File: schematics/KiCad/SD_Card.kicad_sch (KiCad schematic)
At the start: 13 parts, among them J6 Micro_SD_Card_Det_Hirose_DM3AT, U14 LP2950-3.3, U16 74HC4050

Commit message: Update schematics.
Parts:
- renumbered R19 to R20, R20 to R21, R21 to R22, R22 to R23, R23 to R24
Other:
- company: (none) -> By 46nori
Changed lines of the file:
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@@
   (title_block
     (title "Micro SD Card interface")
+    (date "2023-05-03")
+    (company "By 46nori")
   )
   (junction (at 43.18 143.51) (diameter 0) (color 0 0 0 0)
@@
   (symbol (lib_id "power:GND") (at 125.73 71.12 0) (unit 1)
     (in_bom yes) (on_board yes) (dnp no)
-    (property "Reference" "#PWR074" (at 125.73 77.47 0)
+    (property "Reference" "#PWR076" (at 125.73 77.47 0)
       (effects (font (size 1.27 1.27)) hide)
     )
@@
       (project "Z80ATmega128"
         (path "/8c0ff608-9e5b-458c-8fa7-b9973ff97e88/07de70fd-23a2-48ea-a888-9c9311d1e8a8"
-          (reference "#PWR074") (unit 1)
+          (reference "#PWR076") (unit 1)
         )
       )
@@
   (symbol (lib_id "power:GND") (at 73.66 96.52 0) (unit 1)
     (in_bom yes) (on_board yes) (dnp no) (fields_autoplaced)
-    (property "Reference" "#PWR075" (at 73.66 102.87 0)
+    (property "Reference" "#PWR077" (at 73.66 102.87 0)
       (effects (font (size 1.27 1.27)) hide)
     )
@@
       (project "Z80ATmega128"
         (path "/8c0ff608-9e5b-458c-8fa7-b9973ff97e88/07de70fd-23a2-48ea-a888-9c9311d1e8a8"
-          (reference "#PWR075") (unit 1)
+          (reference "#PWR077") (unit 1)
         )
       )
@@
   (symbol (lib_id "power:GND") (at 148.59 168.91 0) (unit 1)
     (in_bom yes) (on_board yes) (dnp no) (fields_autoplaced)
-    (property "Reference" "#PWR081" (at 148.59 175.26 0)
+    (property "Reference" "#PWR083" (at 148.59 175.26 0)
       (effects (font (size 1.27 1.27)) hide)
     )
@@
       (project "Z80ATmega128"
         (path "/8c0ff608-9e5b-458c-8fa7-b9973ff97e88/07de70fd-23a2-48ea-a888-9c9311d1e8a8"
-          (reference "#PWR081") (unit 1)
+          (reference "#PWR083") (unit 1)
         )
       )
@@
   (symbol (lib_id "Device:R") (at 90.17 44.45 0) (unit 1)
     (in_bom yes) (on_board yes) (dnp no) (fields_autoplaced)
-    (property "Reference" "R19" (at 92.71 43.1799 0)
+    (property "Reference" "R20" (at 92.71 43.1799 0)
       (effects (font (size 1.27 1.27)) (justify left))
     )
@@
       (project "Z80ATmega128"
         (path "/8c0ff608-9e5b-458c-8fa7-b9973ff97e88/07de70fd-23a2-48ea-a888-9c9311d1e8a8"
-          (reference "R19") (unit 1)
+          (reference "R20") (unit 1)
         )
       )
@@
   (symbol (lib_id "power:+3.3V") (at 123.19 146.05 0) (unit 1)
     (in_bom yes) (on_board yes) (dnp no) (fields_autoplaced)
-    (property "Reference" "#PWR080" (at 123.19 149.86 0)
+    (property "Reference" "#PWR082" (at 123.19 149.86 0)
       (effects (font (size 1.27 1.27)) hide)
     )
@@
       (project "Z80ATmega128"
         (path "/8c0ff608-9e5b-458c-8fa7-b9973ff97e88/07de70fd-23a2-48ea-a888-9c9311d1e8a8"
-          (reference "#PWR080") (unit 1)
+          (reference "#PWR082") (unit 1)
         )
       )
@@
   (symbol (lib_id "Device:R") (at 148.59 95.25 0) (unit 1)
     (in_bom yes) (on_board yes) (dnp no) (fields_autoplaced)
-    (property "Reference" "R22" (at 151.13 93.9799 0)
+    (property "Reference" "R23" (at 151.13 93.9799 0)
       (effects (font (size 1.27 1.27)) (justify left))
     )
@@
       (project "Z80ATmega128"
         (path "/8c0ff608-9e5b-458c-8fa7-b9973ff97e88/07de70fd-23a2-48ea-a888-9c9311d1e8a8"
-          (reference "R22") (unit 1)
+          (reference "R23") (unit 1)
         )
       )
@@
         )
         (path "/8c0ff608-9e5b-458c-8fa7-b9973ff97e88/07de70fd-23a2-48ea-a888-9c9311d1e8a8"
-          (reference "#PWR079") (unit 1)
+          (reference "#PWR081") (unit 1)
         )
       )
@@
   (symbol (lib_id "power:+3.3V") (at 73.66 40.64 0) (unit 1)
     (in_bom yes) (on_board yes) (dnp no)
-    (property "Reference" "#PWR071" (at 73.66 44.45 0)
+    (property "Reference" "#PWR073" (at 73.66 44.45 0)
       (effects (font (size 1.27 1.27)) hide)
     )
@@
       (project "Z80ATmega128"
         (path "/8c0ff608-9e5b-458c-8fa7-b9973ff97e88/07de70fd-23a2-48ea-a888-9c9311d1e8a8"
-          (reference "#PWR071") (unit 1)
+          (reference "#PWR073") (unit 1)
         )
       )
@@
   (symbol (lib_id "Device:R") (at 125.73 44.45 0) (unit 1)
     (in_bom yes) (on_board yes) (dnp no) (fields_autoplaced)
-    (property "Reference" "R20" (at 128.27 43.1799 0)
+    (property "Reference" "R21" (at 128.27 43.1799 0)
       (effects (font (size 1.27 1.27)) (justify left))
     )
@@
       (project "Z80ATmega128"
         (path "/8c0ff608-9e5b-458c-8fa7-b9973ff97e88/07de70fd-23a2-48ea-a888-9c9311d1e8a8"
-          (reference "R20") (unit 1)
+          (reference "R21") (unit 1)
         )
       )
@@
   (symbol (lib_id "Device:R") (at 116.84 100.33 270) (unit 1)
     (in_bom yes) (on_board yes) (dnp no) (fields_autoplaced)
-    (property "Reference" "R23" (at 116.84 93.98 90)
+    (property "Reference" "R24" (at 116.84 93.98 90)
       (effects (font (size 1.27 1.27)))
     )
@@
       (project "Z80ATmega128"
         (path "/8c0ff608-9e5b-458c-8fa7-b9973ff97e88/07de70fd-23a2-48ea-a888-9c9311d1e8a8"
-          (reference "R23") (unit 1)
+          (reference "R24") (unit 1)
         )
       )
@@
   (symbol (lib_id "power:VCC") (at 125.73 40.64 0) (unit 1)
     (in_bom yes) (on_board yes) (dnp no) (fields_autoplaced)
-    (property "Reference" "#PWR073" (at 125.73 44.45 0)
+    (property "Reference" "#PWR075" (at 125.73 44.45 0)
       (effects (font (size 1.27 1.27)) hide)
     )
@@
       (project "Z80ATmega128"
         (path "/8c0ff608-9e5b-458c-8fa7-b9973ff97e88/07de70fd-23a2-48ea-a888-9c9311d1e8a8"
-          (reference "#PWR073") (unit 1)
+          (reference "#PWR075") (unit 1)
         )
       )
@@
         )
         (path "/8c0ff608-9e5b-458c-8fa7-b9973ff97e88/07de70fd-23a2-48ea-a888-9c9311d1e8a8"
-          (reference "#PWR077") (unit 1)
+          (reference "#PWR079") (unit 1)
         )
       )
@@
   (symbol (lib_id "Device:R") (at 125.73 67.31 0) (unit 1)
     (in_bom yes) (on_board yes) (dnp no) (fields_autoplaced)
-    (property "Reference" "R21" (at 128.27 66.0399 0)
+    (property "Reference" "R22" (at 128.27 66.0399 0)
       (effects (font (size 1.27 1.27)) (justify left))
     )
@@
       (project "Z80ATmega128"
         (path "/8c0ff608-9e5b-458c-8fa7-b9973ff97e88/07de70fd-23a2-48ea-a888-9c9311d1e8a8"
-          (reference "R21") (unit 1)
+          (reference "R22") (unit 1)
         )
       )
@@
   (symbol (lib_id "power:GND") (at 123.19 171.45 0) (unit 1)
     (in_bom yes) (on_board yes) (dnp no) (fields_autoplaced)
-    (property "Reference" "#PWR082" (at 123.19 177.8 0)
+    (property "Reference" "#PWR084" (at 123.19 177.8 0)
       (effects (font (size 1.27 1.27)) hide)
     )
@@
       (project "Z80ATmega128"
         (path "/8c0ff608-9e5b-458c-8fa7-b9973ff97e88/07de70fd-23a2-48ea-a888-9c9311d1e8a8"
-          (reference "#PWR082") (unit 1)
+          (reference "#PWR084") (unit 1)
         )
       )
@@
   (symbol (lib_id "power:GND") (at 148.59 100.33 0) (unit 1)
     (in_bom yes) (on_board yes) (dnp no) (fields_autoplaced)
-    (property "Reference" "#PWR076" (at 148.59 106.68 0)
+    (property "Reference" "#PWR078" (at 148.59 106.68 0)
       (effects (font (size 1.27 1.27)) hide)
     )
@@
       (project "Z80ATmega128"
         (path "/8c0ff608-9e5b-458c-8fa7-b9973ff97e88/07de70fd-23a2-48ea-a888-9c9311d1e8a8"
-          (reference "#PWR076") (unit 1)
+          (reference "#PWR078") (unit 1)
         )
       )
@@
   (symbol (lib_id "power:VCC") (at 90.17 40.64 0) (unit 1)
     (in_bom yes) (on_board yes) (dnp no)
-    (property "Reference" "#PWR072" (at 90.17 44.45 0)
+    (property "Reference" "#PWR074" (at 90.17 44.45 0)
       (effects (font (size 1.27 1.27)) hide)
     )
@@
       (project "Z80ATmega128"
         (path "/8c0ff608-9e5b-458c-8fa7-b9973ff97e88/07de70fd-23a2-48ea-a888-9c9311d1e8a8"
-          (reference "#PWR072") (unit 1)
+          (reference "#PWR074") (unit 1)
         )
       )
@@
         )
         (path "/8c0ff608-9e5b-458c-8fa7-b9973ff97e88/07de70fd-23a2-48ea-a888-9c9311d1e8a8"
-          (reference "#PWR078") (unit 1)
-        )
-      )
+          (reference "#PWR080") (unit 1)
+        )
+      )

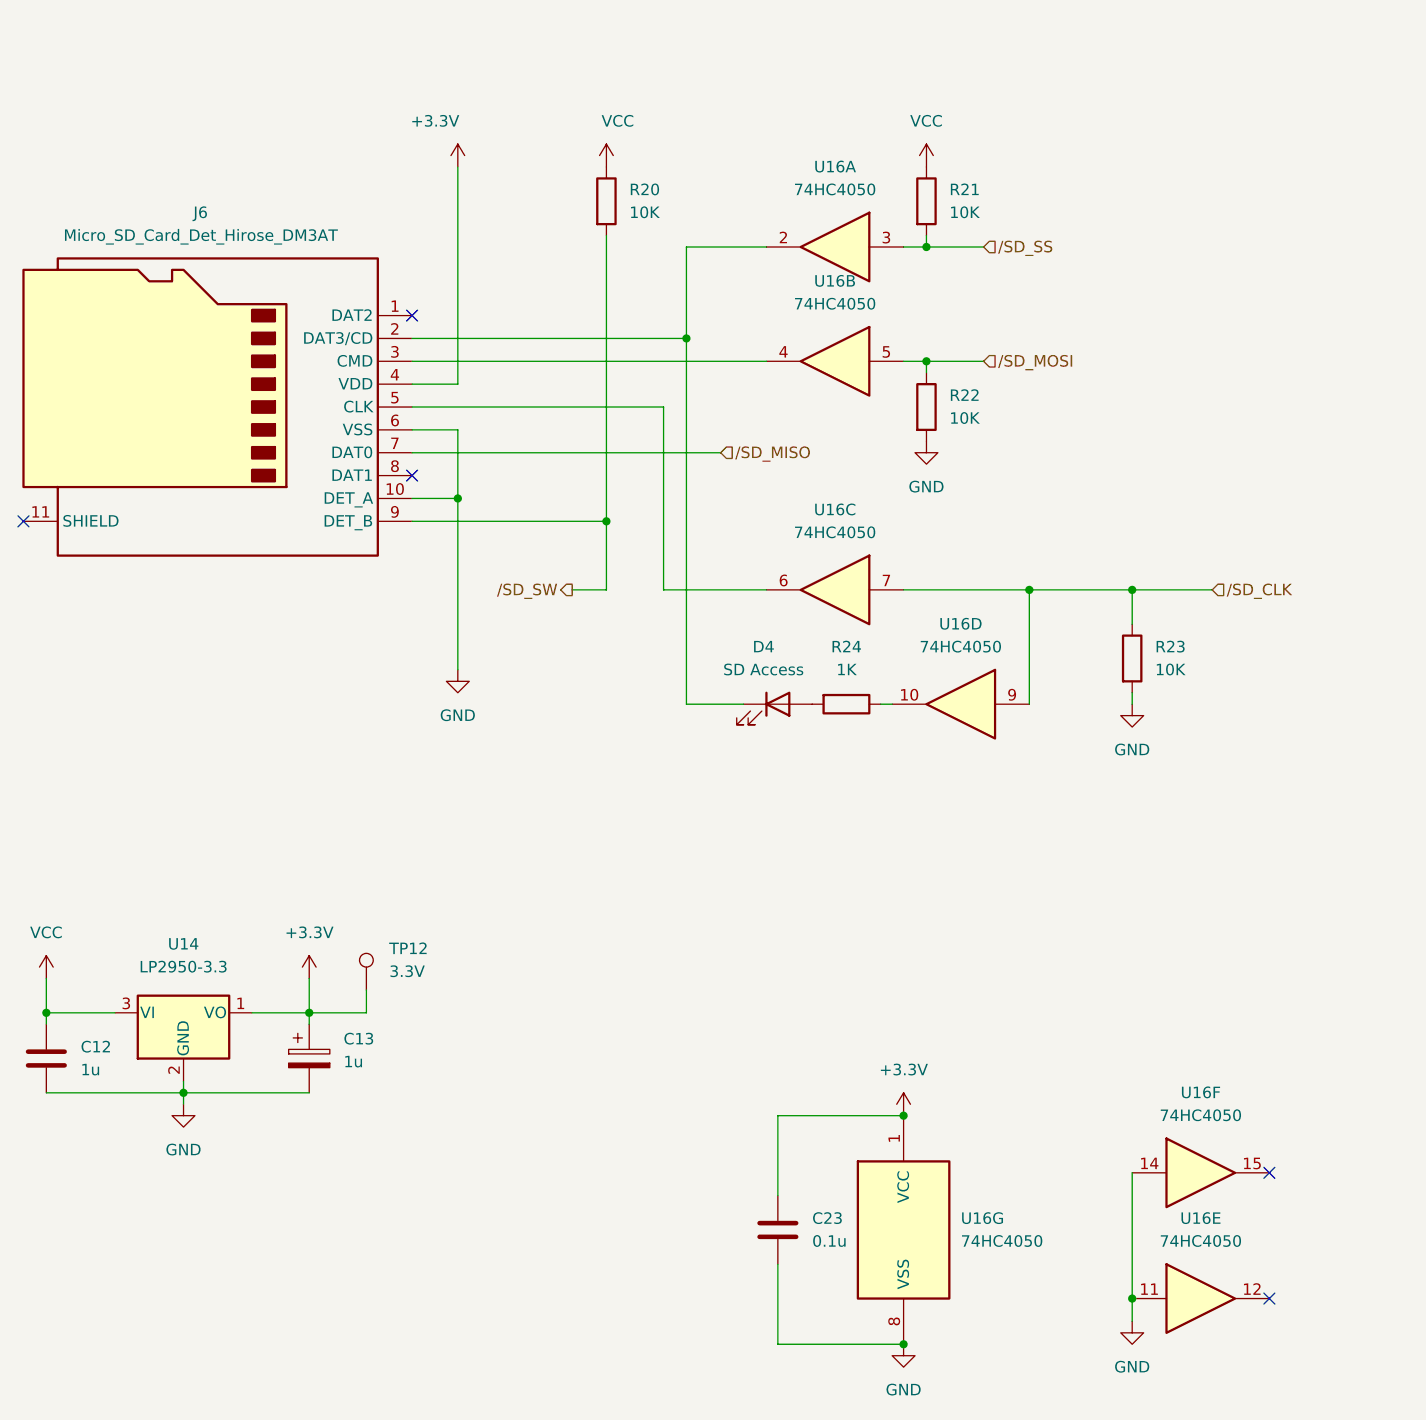
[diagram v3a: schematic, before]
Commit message: Update RESET circuit using DS1232N.
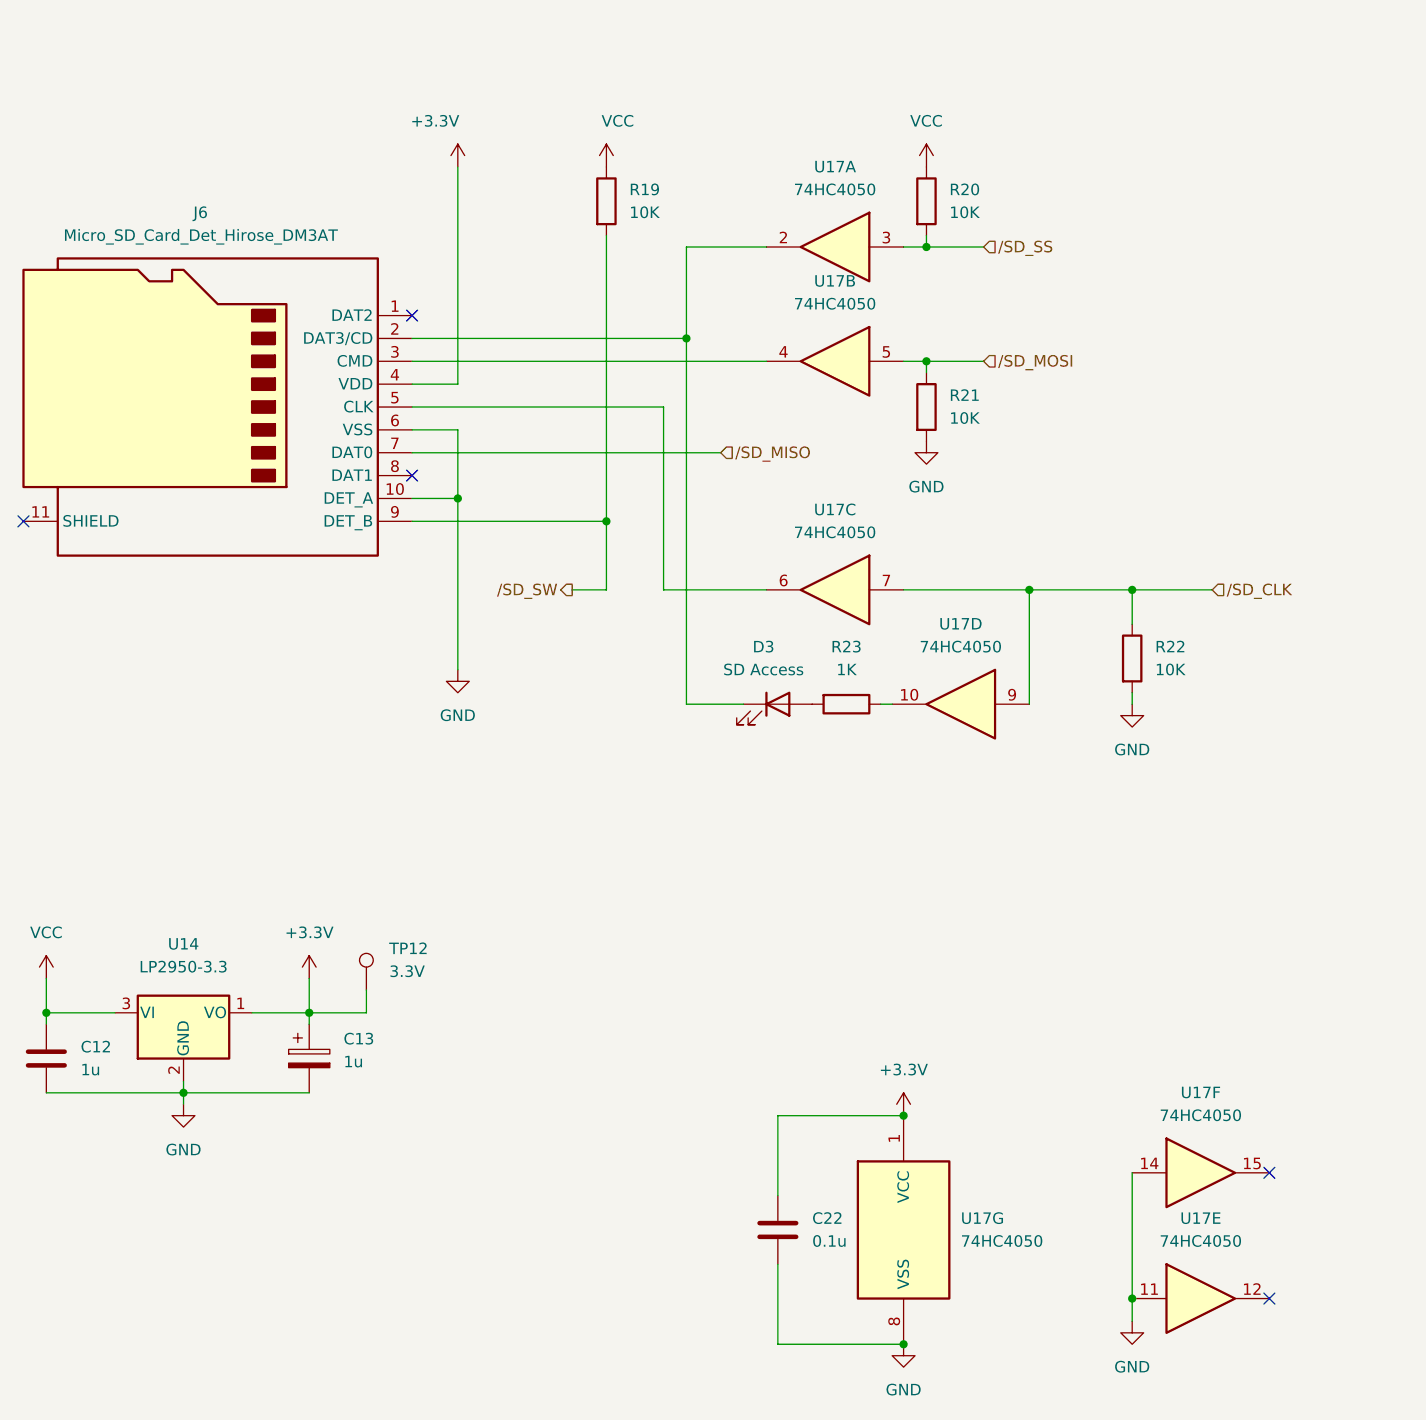
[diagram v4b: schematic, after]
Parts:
- renumbered C23 to C22, D4 to D3, R20 to R19, R21 to R20, R22 to R21, R23 to R22, R24 to R23, U16 to U17

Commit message: Fixed bug of WAIT generator circuit
Clock circuit is moved to 2nd layer.
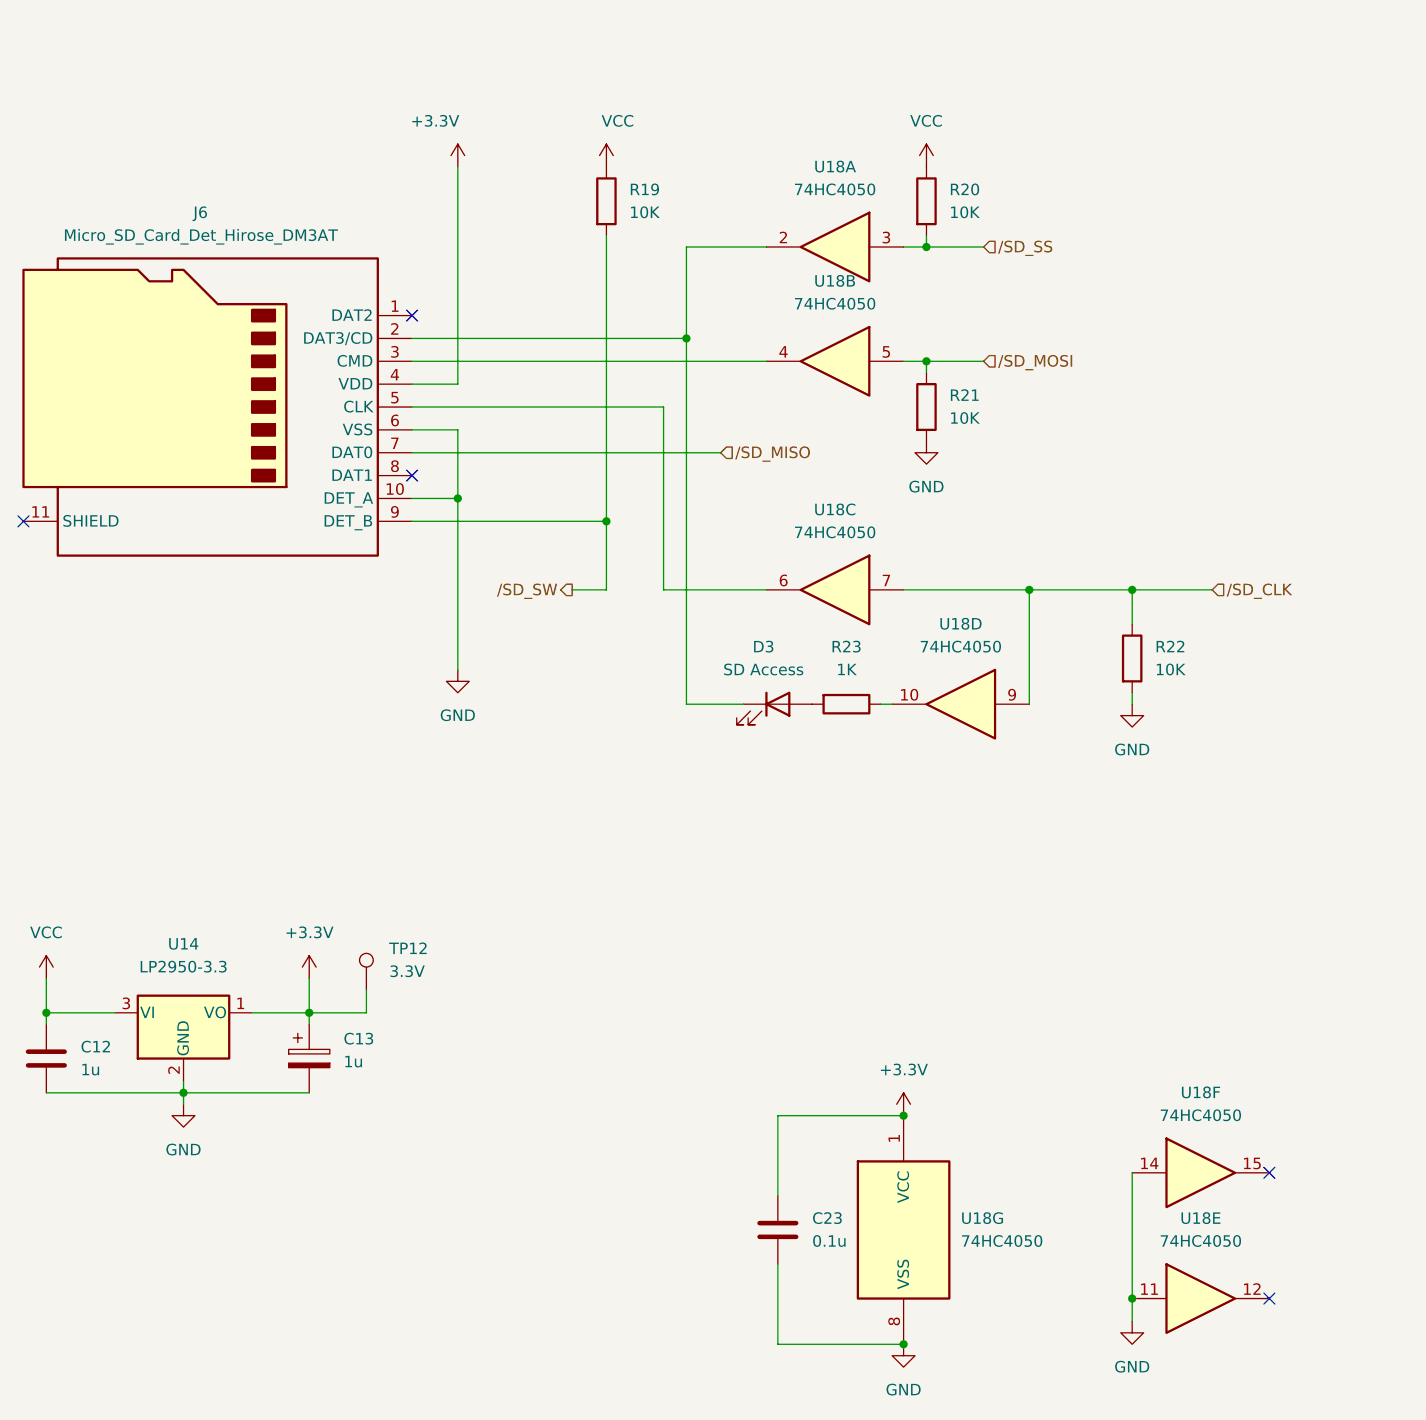
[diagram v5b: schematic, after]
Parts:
- renumbered C22 to C23, U17 to U18
